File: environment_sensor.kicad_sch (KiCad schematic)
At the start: 119 parts, among them J17 USB-C_GCT_USB4145-03-0070-C, J18 JST_SH_1x4_SM04B-SRSS-TB-LF-SN, U11 FT4232H_VQFN, U27 AP7370-33SA-7, U28 STM32G474CET6, U29 MB85RC1MTPNF-G, U30 SHT45, U31 BME280, Y2 Resonator_12MHz_ABM3B, Y3 Resonator_32.768kHz_ECX-31B, Y4 Resonator_8MHz_ABM3B

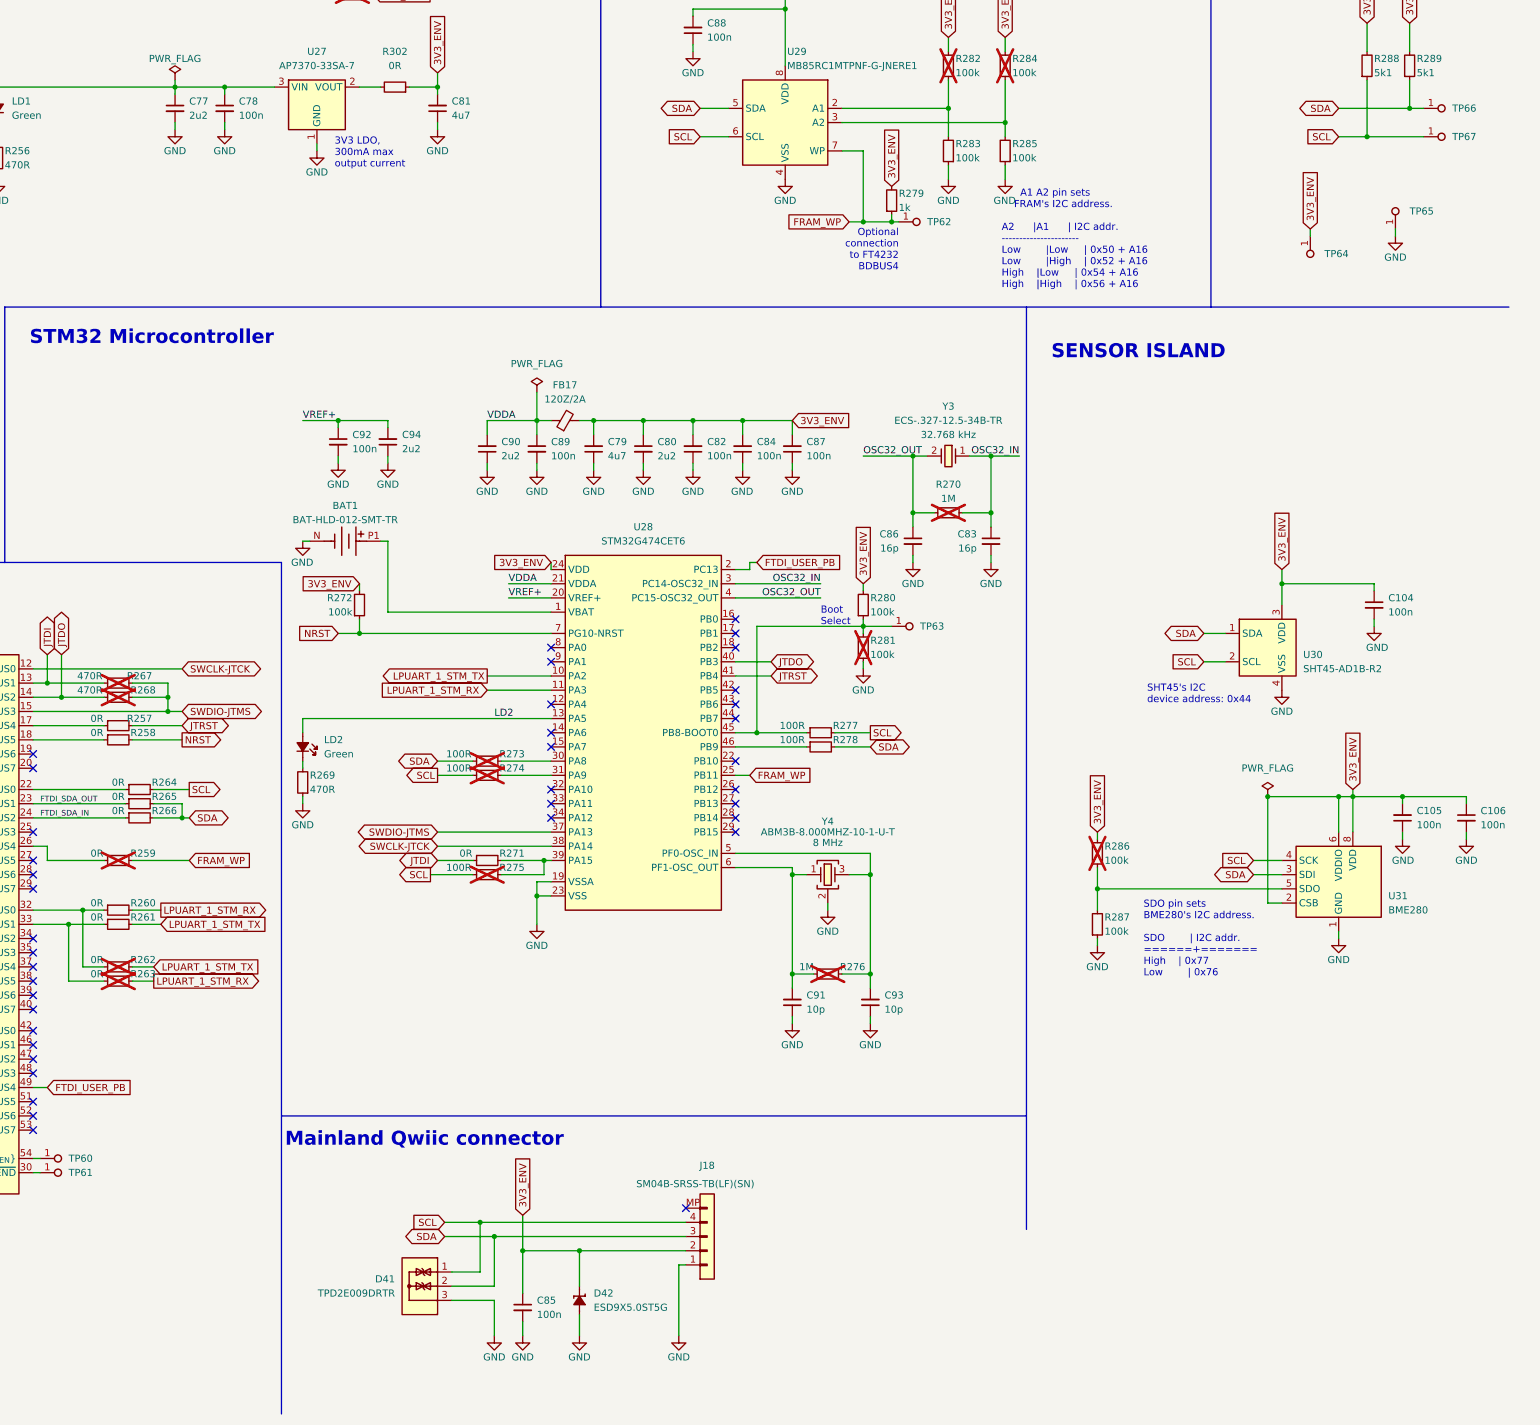
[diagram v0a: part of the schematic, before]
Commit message: [#62160] Split i2c buses to env and backplane
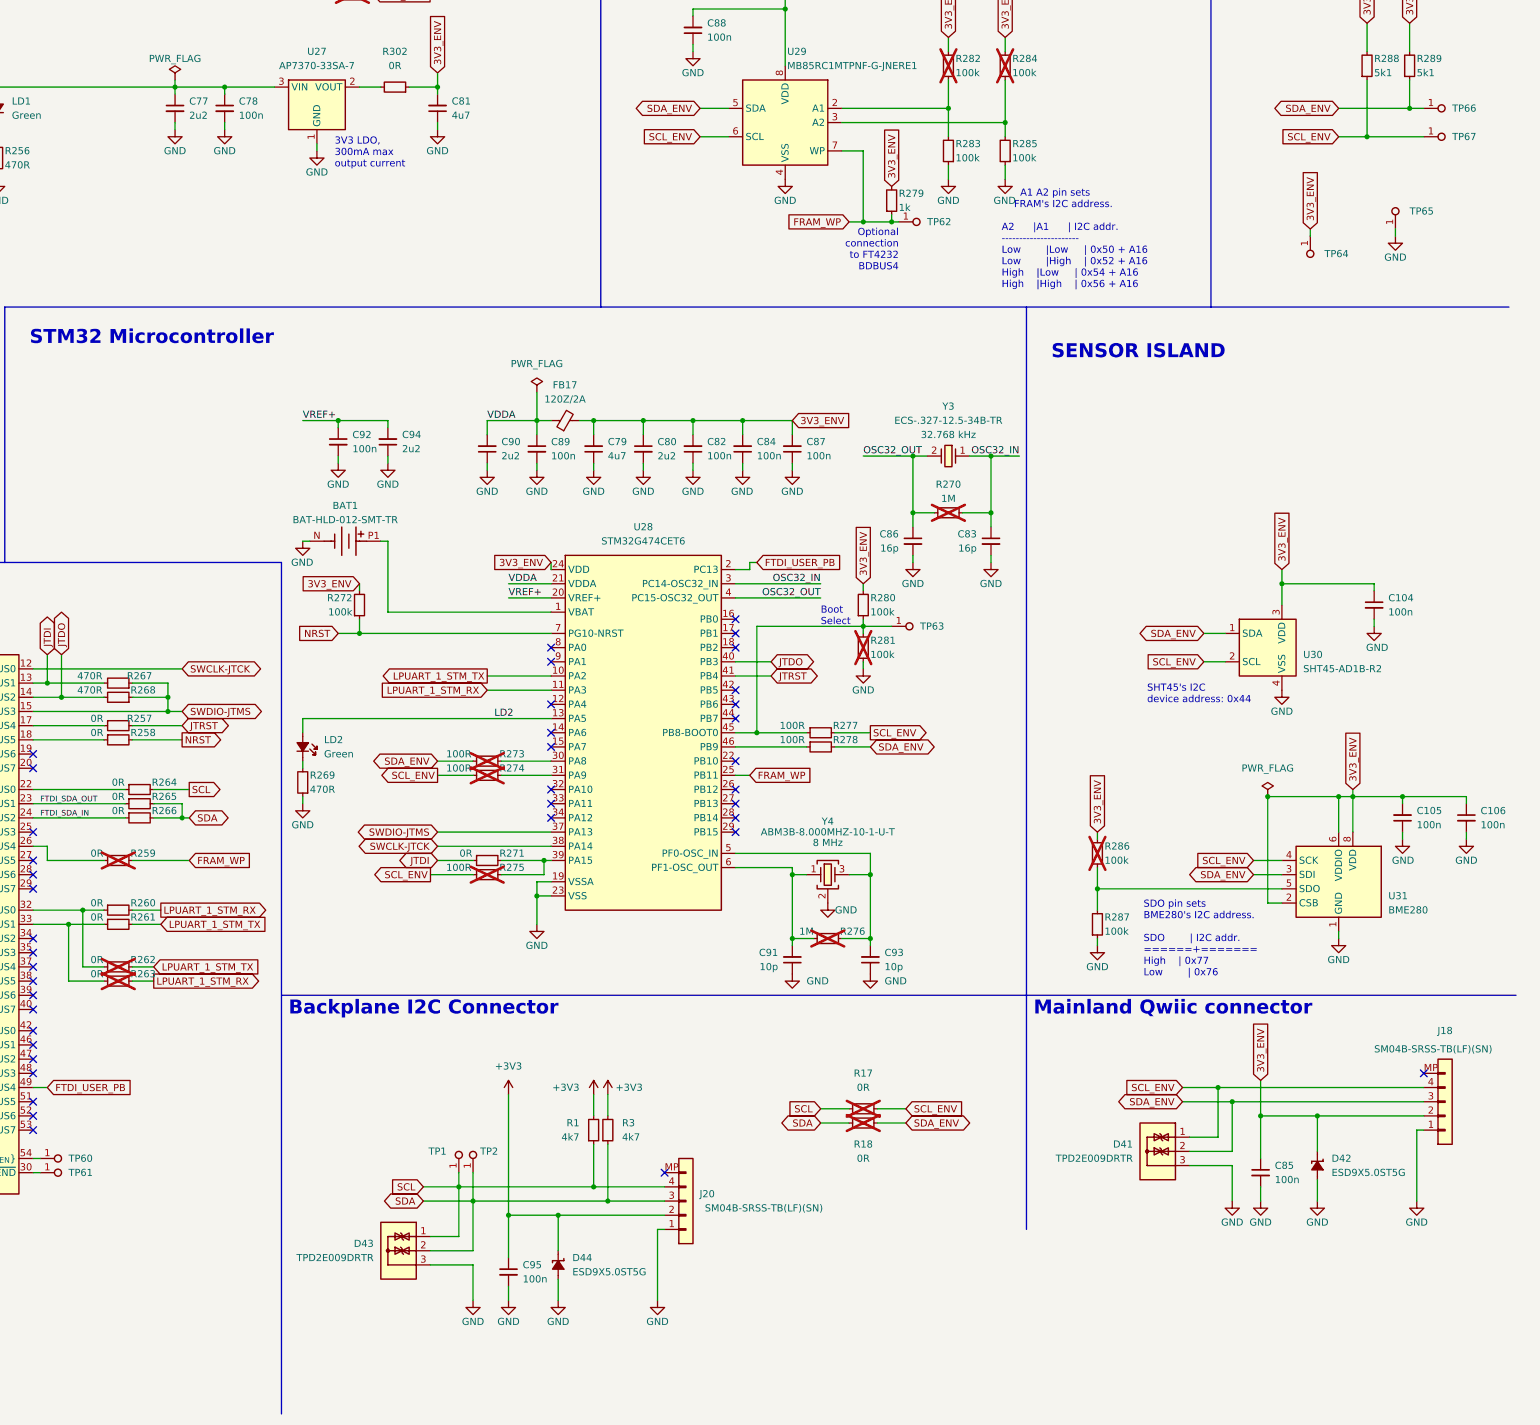
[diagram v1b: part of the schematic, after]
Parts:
- added C95: C_100n_0402, antmicro-footprints:C_0402_1005Metric, symbol antmicroCapacitors0402:C_100n_0402
- added D43: TPD2E009_SOT-9X3, antmicro-footprints:SOT-723, symbol antmicroTVSDiodes:TPD2E009_SOT-9X3
- added D44: ESD9X5.0ST5G, antmicro-footprints:SOD-923, symbol antmicroTVSDiodes:ESD9X5.0ST5G
- added J20: JST_SH_1x4_SM04B-SRSS-TB-LF-SN, antmicro-footprints:Conn_JST_SH_1x4_SM04B-SRSS-TB-LF-SN, symbol antmicroWire2BoardConnectors:JST_SH_1x4_SM04B-SRSS-TB-LF-SN
- added R1, R3: R_4k7_0402, antmicro-footprints:R_0402_1005Metric, symbol antmicroResistors0402:R_4k7_0402
- added R17, R18: R_0R_0402, antmicro-footprints:R_0402_1005Metric, symbol antmicroResistors0402:R_0R_0402
- added TP1, TP2: TP_1mm_SMD, antmicro-footprints:TP_SMD_1mm, symbol antmicroTestPoints:TP_1mm_SMD
- R267, R268: now fitted
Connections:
- net +3V3: now also C95.1, D44.1 (C), J20.2, R1.2, R3.2
- net GND: now also C95.2, D43.3, D44.2 (A), J20.1
- net SCL: now also D43.1, J20.4, R1.1, R17.1, TP1.1; no longer D41.1, J18.4, R274.2, R275.2, R277.2, R288.1, TP67.1, U29.6 (SCL), U30.2 (SCL), U31.4 (SCK)
- net SDA: now also D43.2, J20.3, R18.1, R3.1, TP2.1; no longer D41.2, J18.3, R273.2, R278.2, R289.1, TP66.1, U29.5 (SDA), U30.1 (SDA), U31.3 (SDI)
- new net SCL_ENV: D41.1, J18.4, R17.2, R274.2, R275.2, R277.2, R288.1, TP67.1, U29.6 (SCL), U30.2 (SCL), U31.4 (SCK)
- new net SDA_ENV: D41.2, J18.3, R18.2, R273.2, R278.2, R289.1, TP66.1, U29.5 (SDA), U30.1 (SDA), U31.3 (SDI)
- no-connect marks 47 -> 48
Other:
- note added: "Backplane I2C Connector"
- moved on the sheet: C85, C91, C93, D41, D42, J18, R276

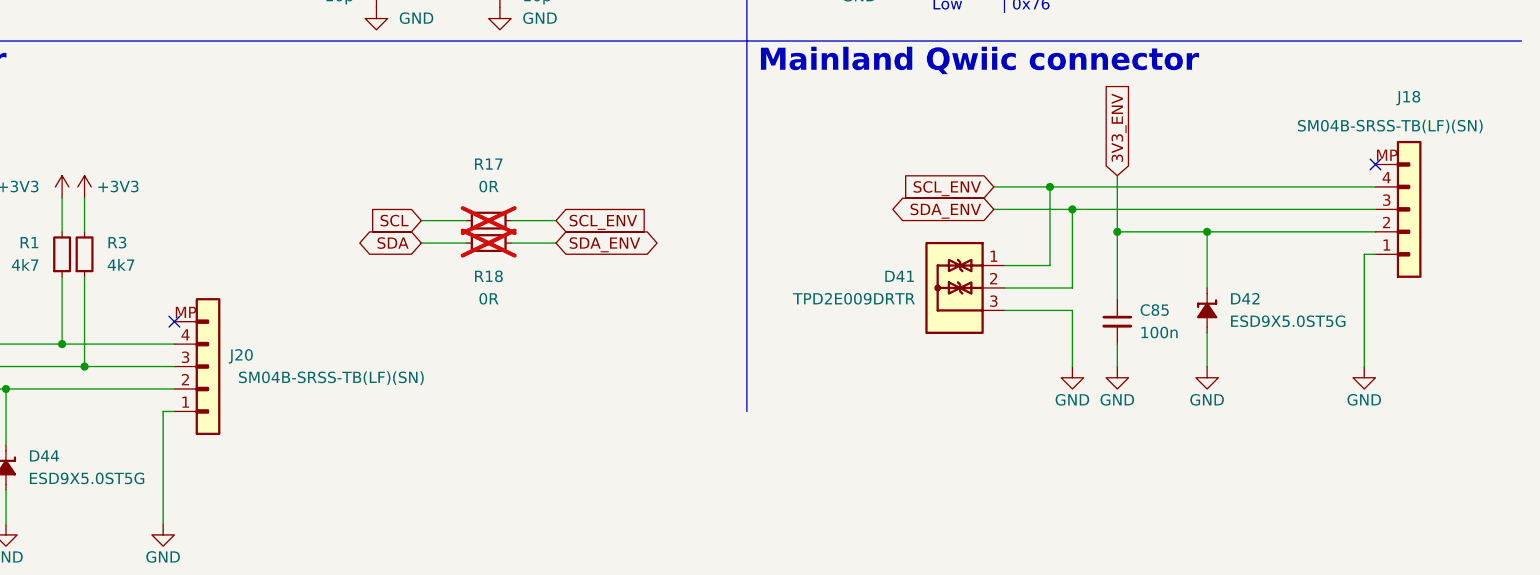
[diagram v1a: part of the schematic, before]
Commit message: [#62160] Fix unconnected
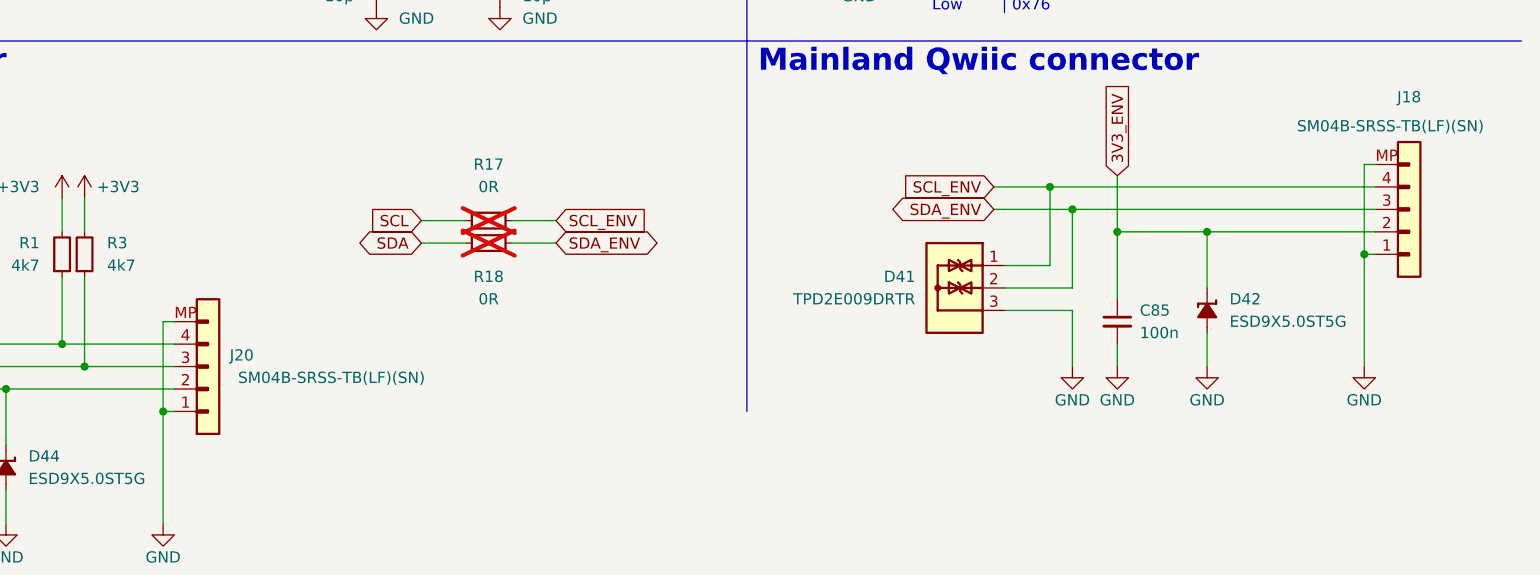
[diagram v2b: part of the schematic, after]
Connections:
- net GND: now also J18.MP, J20.MP
- no-connect marks 48 -> 46
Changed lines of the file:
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@@
   (junction (at 40.64 204.47) (diameter 0) (color 0 0 0 0)
   )
+  (junction (at 254 252.73) (diameter 0) (color 0 0 0 0)
+  )
   (junction (at 114.3 52.07) (diameter 0) (color 0 0 0 0)
   )
@@
   )
   (junction (at 168.91 179.07) (diameter 0) (color 0 0 0 0)
+  )
+  (junction (at 389.89 234.95) (diameter 0) (color 0 0 0 0)
   )
   (junction (at 69.85 48.26) (diameter 0) (color 0 0 0 0)
@@
   (no_connect (at 234.95 151.13))
   (no_connect (at 101.6 199.39))
-  (no_connect (at 255.27 242.57))
   (no_connect (at 44.45 62.23))
   (no_connect (at 267.97 168.91))
@@
   (no_connect (at 101.6 196.85))
   (no_connect (at 130.81 276.86))
-  (no_connect (at 391.16 224.79))
   (no_connect (at 267.97 148.59))
   (no_connect (at 142.24 167.64))
@@
     (stroke (width 0) (type default))
   )
+  (wire (pts (xy 389.89 224.79) (xy 389.89 234.95))
+    (stroke (width 0) (type default))
+  )
   (wire (pts (xy 306.07 39.37) (xy 306.07 41.91))
     (stroke (width 0) (type default))
@@
     (stroke (width 0) (type default))
   )
+  (wire (pts (xy 391.16 224.79) (xy 389.89 224.79))
+    (stroke (width 0) (type default))
+  )
   (wire (pts (xy 287.02 52.07) (xy 306.07 52.07))
+    (stroke (width 0) (type default))
+  )
+  (wire (pts (xy 255.27 242.57) (xy 254 242.57))
     (stroke (width 0) (type default))
   )
@@
     (stroke (width 0) (type default))
   )
+  (wire (pts (xy 254 242.57) (xy 254 252.73))
+    (stroke (width 0) (type default))
+  )

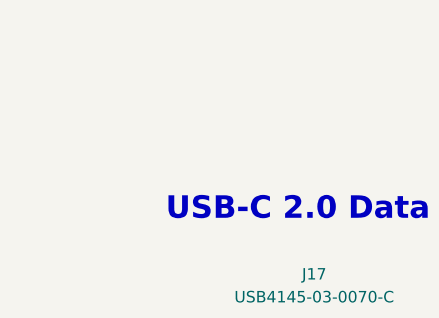
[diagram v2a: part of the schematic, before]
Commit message: [#62160] Apply dnp to pcb
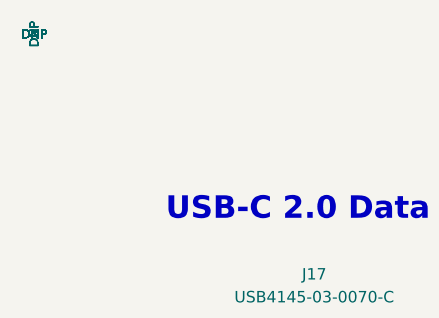
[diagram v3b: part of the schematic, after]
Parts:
- H10, H11, H12, R17, R18, R250, R252, R259, R262, R263, R270, R273, R274, R275, R276, R281, R282, R284, R286, R290: DNP (none) -> DNP; now left out of the parts list
